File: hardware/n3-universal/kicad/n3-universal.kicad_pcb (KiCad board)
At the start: 2 copper layers, 278 x 120 mm, 131 parts, among them J1 Bornier_5.08, J10 JST-XH, J11 Bornier_5.08, J12 Bornier_5.08, J13 Support OLED, J14 Support I2C ext, J15 Header servo, J16 Header servo, J17 Header service, J18 Bornier_5.08, J19 Bornier_5.08, J2 Jack 5.5/2.1, J20 Header alim, J21 Support I2C libre, J22 Support I2C libre, J23 Bornier_5.08, J24 Bornier_5.08, J25 Bornier_5.08, J26 Bornier_5.08, J27 Bornier_5.08, J28 Support I2C libre, J29 JST-XH, J3 Bornier_5.08, J30 JST-XH, J31 Bornier_5.08, J32 Bornier_5.08, J33 Bornier_5.08, J34 Bornier_5.08, J35 Support module microSD, J36 Bornier_5.08, J37 Bornier_5.08, J4 Bornier_5.08, J5 Bornier_5.08, J6 Bornier_5.08, J7 JST-XH, J8 JST-XH, J9 JST-XH, K1 SRD-05VDC-SL-C, K2 SRD-05VDC-SL-C, K3 SRD-05VDC-SL-C, K4 SRD-05VDC-SL-C, K5 SRD-05VDC-SL-C, K6 SRD-05VDC-SL-C, Q1 BC337-40, Q10 BC337-40, Q11 NDP6020P, Q2 BC337-40, Q3 BC337-40, Q4 BC337-40, Q5 BC337-40, Q6 BC337-40, Q7 NDP6020P, Q8 BC337-40, Q9 BS250

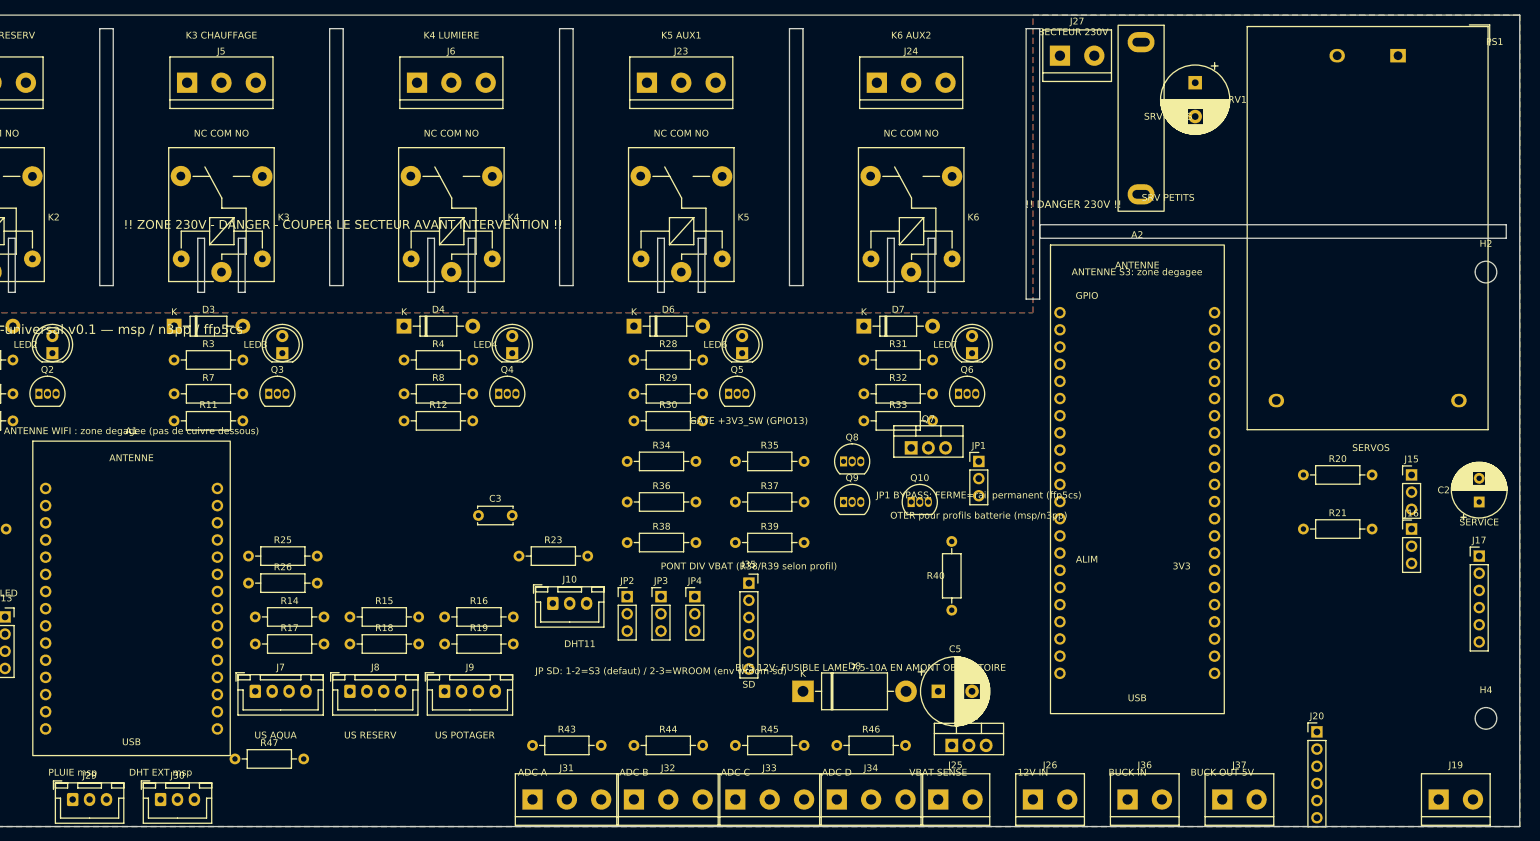
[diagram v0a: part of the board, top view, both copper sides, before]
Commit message: fix(n3-universal): géométrie secteur sans croisement, contour réparé, passe de placement complète
PSU : J27/F1/RV1 hors du corps du Hi-Link (décalé à x303), pistes L/N/LF
redessinées sans croisement ni court (varistance re-câblée N/LF), fente
frontière y71-73 disjointe de la fente verticale (contour valide). ~30
repositionnements sur courtyards réels (rangée basse de borniers y151,
colonne gate/diviseur/SD décalée hors des canaux relais 5/6 et du bloc DHT,
servos/J17/J20 rive droite, trous de fixation déplacés hors zone secteur).
ERC 0 erreur, garde anti-dérive vert, 1 seul avertissement de recouvrement
résiduel corrigé. Routage v2 en cours.

Co-Authored-By: Claude <noreply@anthropic.com>
Claude-Session: https://claude.ai/code/session_01HcxShQb65yktRwp31wBq9q
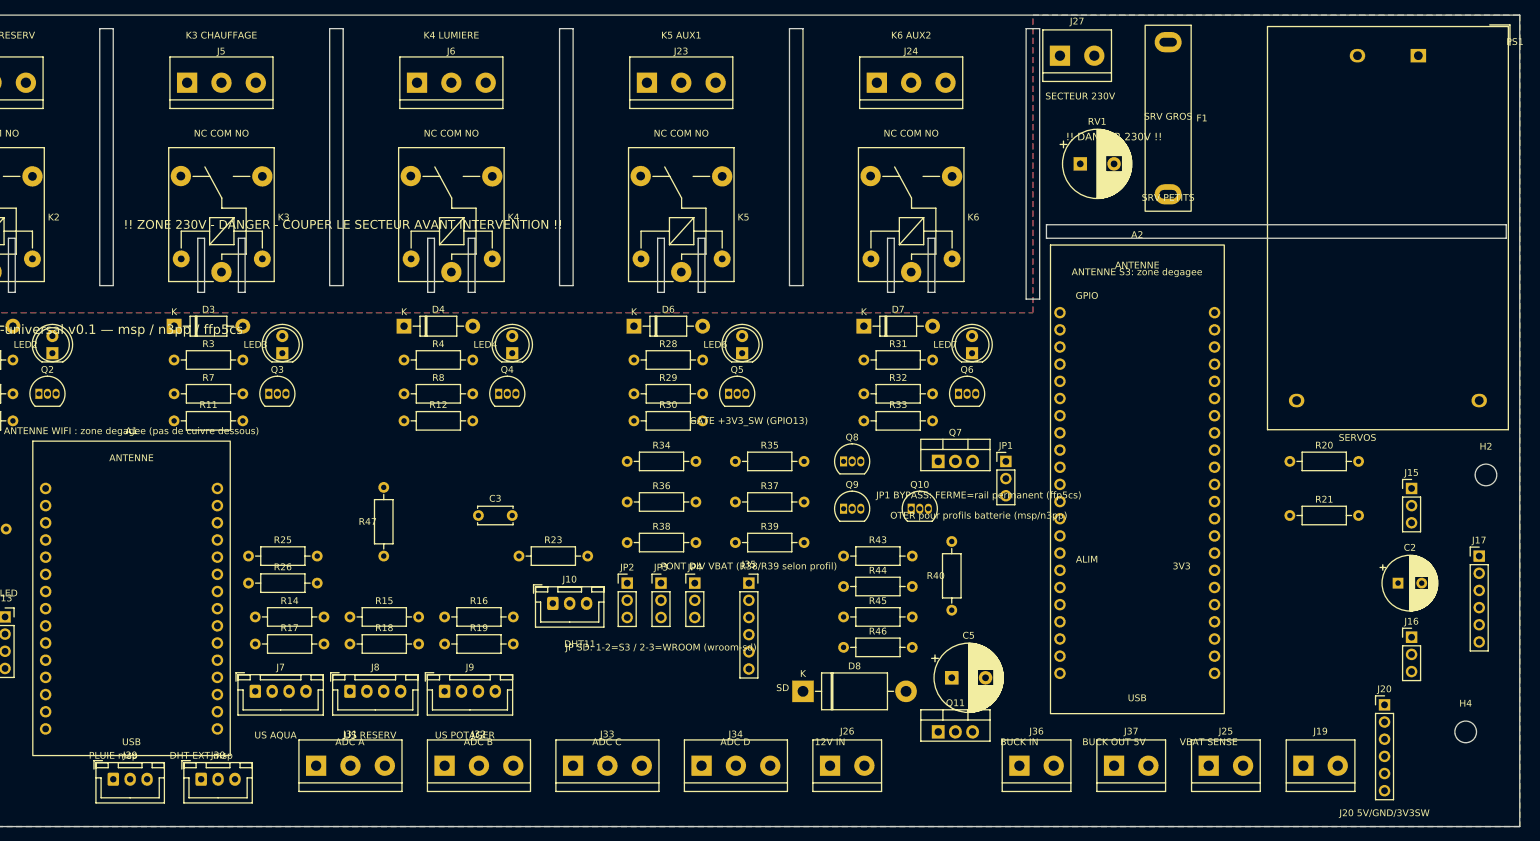
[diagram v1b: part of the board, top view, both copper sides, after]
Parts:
- moved R43 53.9 mm to (218.0, 120.0)
- moved J25 40.3 mm to (272.0, 151.0)
- moved R44 38.9 mm to (218.0, 124.5)
- moved R47 37.2 mm to (150.0, 120.0), turned to 90 degrees
- moved J31 32.4 mm to (140.0, 151.0)
- moved J26 30.4 mm to (216.0, 151.0)
- moved H2 30.0 mm to (313.0, 108.0)
- moved J32 28.4 mm to (159.0, 151.0)
- moved R45 24.8 mm to (218.0, 129.0)
- moved J33 24.5 mm to (178.0, 151.0)
- moved RV1 20.8 mm to (253.0, 62.0), turned to 0 degrees
- moved J19 20.6 mm to (286.0, 151.0)
- moved J34 20.6 mm to (197.0, 151.0)
- moved C2 17.0 mm to (300.0, 124.0), turned to 0 degrees
- moved J36 16.8 mm to (244.0, 151.0)
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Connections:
- RV1 pad 1: MAINS_LF -> MAINS_N
- RV1 pad 2: MAINS_N -> MAINS_LF
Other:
- outline, holes or cut-outs redrawn
- board text added: "J20 5V/GND/3V3SW"
- board text added: "JP SD: 1-2=S3 / 2-3=WROOM (wroom-sd)"
- board text removed: "JP SD: 1-2=S3 (defaut) / 2-3=WROOM (env wroom-sd)"
- board text removed: "SERVICE"

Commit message: fix(n3-universal): amorces SEED_TRACKS (port I2C J14/C4 pincé) + C5 hors du courtyard Q11
Co-Authored-By: Claude <noreply@anthropic.com>
Claude-Session: https://claude.ai/code/session_01HcxShQb65yktRwp31wBq9q
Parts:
- moved C5 2.00 mm to (234.0, 136.0)
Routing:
- net +3V3_SW: track 0.00 -> 7.00 mm
- net I2C_SDA: track 0.00 -> 3.50 mm
- net I2C_SCL: track 0.00 -> 3.50 mm

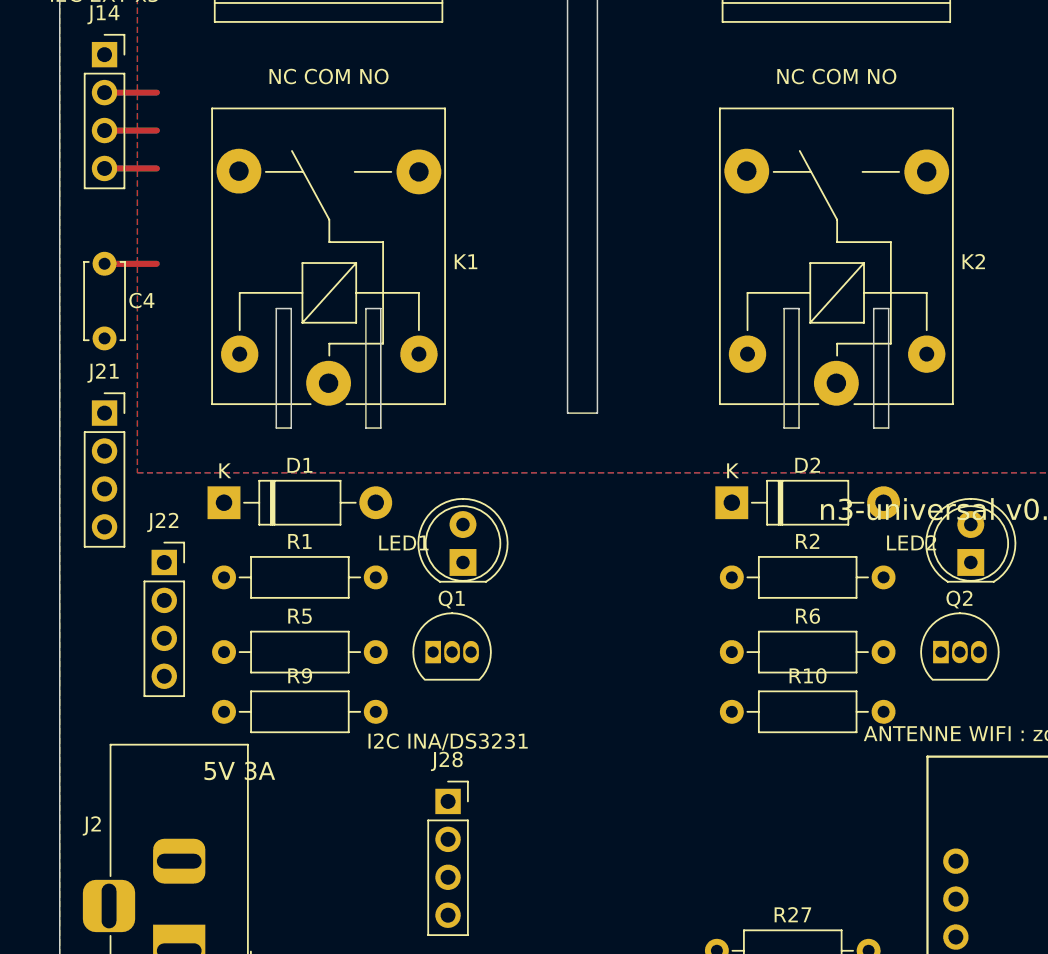
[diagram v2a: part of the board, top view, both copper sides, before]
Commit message: fix(n3-universal): colonne I2C gauche câblée en dur + échappée EN (SEED_TRACKS v2)
Co-Authored-By: Claude <noreply@anthropic.com>
Claude-Session: https://claude.ai/code/session_01HcxShQb65yktRwp31wBq9q
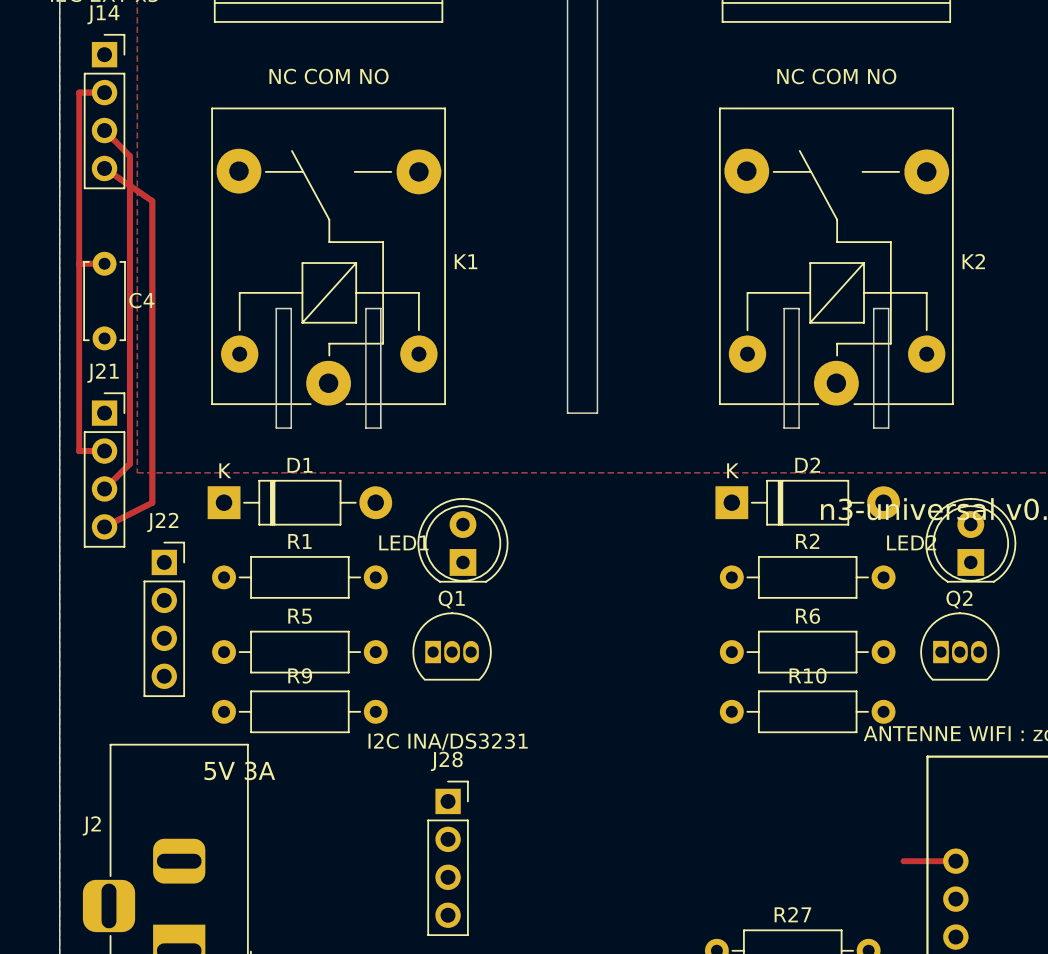
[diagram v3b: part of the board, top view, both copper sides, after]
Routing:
- net I2C_SDA: track 3.50 -> 27.7 mm
- net +3V3_SW: track 7.00 -> 29.1 mm
- net I2C_SCL: track 3.50 -> 25.4 mm
- net EN: track 0.00 -> 3.50 mm
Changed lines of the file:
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@@
 			(layer "F.Fab")
 		)
-		(fp_text user "1"
-			(at 0 -2.3 0)
+		(fp_text user "${REFERENCE}"
+			(at 7.1 0.025 0)
 			(layer "F.Fab")
 			(effects
@@
 			)
 		)
-		(fp_text user "${REFERENCE}"
-			(at 7.1 0.025 0)
+		(fp_text user "1"
+			(at 0 -2.3 0)
 			(layer "F.Fab")
 			(effects
@@
 			)
 		)
-		(fp_text user "${REFERENCE}"
-			(at 5.47 0 0)
+		(fp_text user "K"
+			(at 0 -2.1 0)
 			(layer "F.Fab")
 			(effects
@@
 			)
 		)
-		(fp_text user "K"
-			(at 0 -2.1 0)
+		(fp_text user "${REFERENCE}"
+			(at 5.47 0 0)
 			(layer "F.Fab")
 			(effects
@@
 			)
 		)
-		(fp_text user "K"
-			(at 0 -2.1 0)
+		(fp_text user "${REFERENCE}"
+			(at 5.47 0 0)
 			(layer "F.Fab")
 			(effects
@@
 			)
 		)
-		(fp_text user "${REFERENCE}"
-			(at 5.47 0 0)
+		(fp_text user "K"
+			(at 0 -2.1 0)
 			(layer "F.Fab")
 			(effects
@@
 			)
 		)
-		(fp_text user "${REFERENCE}"
-			(at 8.3325 0 0)
+		(fp_text user "K"
+			(at 0 -2.6 0)
 			(layer "F.Fab")
 			(effects
@@
 			)
 		)
-		(fp_text user "K"
-			(at 0 -2.6 0)
+		(fp_text user "${REFERENCE}"
+			(at 8.3325 0 0)
 			(layer "F.Fab")
 			(effects
@@
 			(layer "F.Fab")
 		)
-		(fp_text user "${REFERENCE}"
-			(at 7.1 0.025 0)
+		(fp_text user "1"
+			(at 0 -2.3 0)
 			(layer "F.Fab")
 			(effects
@@
 			)
 		)
-		(fp_text user "1"
-			(at 0 -2.3 0)
+		(fp_text user "${REFERENCE}"
+			(at 7.1 0.025 0)
 			(layer "F.Fab")
 			(effects
@@
 			)
 		)
-		(fp_text user "K"
-			(at 0 -2.1 0)
+		(fp_text user "${REFERENCE}"
+			(at 5.47 0 0)
 			(layer "F.Fab")
 			(effects
@@
 			)
 		)
-		(fp_text user "${REFERENCE}"
-			(at 5.47 0 0)
+		(fp_text user "K"
+			(at 0 -2.1 0)
 			(layer "F.Fab")
 			(effects
@@
 			(layer "F.Fab")
 		)
-		(fp_text user "1"
-			(at 0 -2.3 0)
+		(fp_text user "${REFERENCE}"
+			(at 7.1 0.025 0)
 			(layer "F.Fab")
 			(effects
@@
 			)
 		)
-		(fp_text user "${REFERENCE}"
-			(at 7.1 0.025 0)
+		(fp_text user "1"
+			(at 0 -2.3 0)
 			(layer "F.Fab")
 			(effects
@@
 			(layer "F.CrtYd")
 		)
-		(fp_text user "USB"
-			(at 12.7 37.5 0)
+		(fp_text user "ANTENNE"
+			(at 12.7 -4.5 0)
 			(layer "F.SilkS")
 			(effects
@@
 			)
 		)
-		(fp_text user "ANTENNE"
-			(at 12.7 -4.5 0)
+		(fp_text user "USB"
+			(at 12.7 37.5 0)
 			(layer "F.SilkS")
 			(effects
@@
 			)
 		)
-		(fp_text user "${REFERENCE}"
-			(at 5.47 0 0)
+		(fp_text user "K"
+			(at 0 -2.1 0)
 			(layer "F.Fab")
 			(effects
@@
 			)
 		)
-		(fp_text user "K"
-			(at 0 -2.1 0)
+		(fp_text user "${REFERENCE}"
+			(at 5.47 0 0)
 			(layer "F.Fab")
 			(effects
@@
 			)
 		)
-		(fp_text user "${REFERENCE}"
-			(at 8.3325 0 0)
+		(fp_text user "K"
+			(at 0 -2.6 0)
 			(layer "F.Fab")
 			(effects
@@
 			)
 		)
-		(fp_text user "K"
-			(at 0 -2.6 0)
+		(fp_text user "${REFERENCE}"
+			(at 8.3325 0 0)
 			(layer "F.Fab")
 			(effects
@@
 			(layer "F.Fab")
 		)
-		(fp_text user "1"
-			(at 0 -2.3 0)
+		(fp_text user "${REFERENCE}"
+			(at 7.1 0.025 0)
 			(layer "F.Fab")
 			(effects
@@
 			)
 		)
-		(fp_text user "${REFERENCE}"
-			(at 7.1 0.025 0)
+		(fp_text user "1"
+			(at 0 -2.3 0)
 			(layer "F.Fab")
 			(effects
@@
 	)
 	(segment
+		(start 41.3 82.54)
+		(end 43 82.54)
+		(width 0.4)
+		(layer "F.Cu")
+		(net 2)
+	)
+	(segment
+		(start 41.3 70)
+		(end 41.3 82.54)
+		(width 0.4)
+		(layer "F.Cu")
+		(net 2)
+	)
+	(segment
 		(start 43 58.54)
-		(end 46.5 58.54)
+		(end 41.3 58.54)
+		(width 0.4)
+		(layer "F.Cu")
+		(net 2)
+	)
+	(segment
+		(start 41.3 70)
+		(end 43 70)
 		(width 0.4)
 		(layer "F.Cu")
@@
 	)
 	(segment
-		(start 43 70)
-		(end 46.5 70)
+		(start 41.3 58.54)
+		(end 41.3 70)
 		(width 0.4)
 		(layer "F.Cu")
@@
 	)
 	(segment
+		(start 96.5 110)
+		(end 100 110)
+		(width 0.4)
+		(layer "F.Cu")
+		(net 11)
+	)
+	(segment
+		(start 44.7 83.4)
+		(end 43 85.08)
+		(width 0.4)
+		(layer "F.Cu")
+		(net 16)
+	)
+	(segment
+		(start 44.7 62.8)
+		(end 44.7 83.4)
+		(width 0.4)
+		(layer "F.Cu")
+		(net 16)
+	)
+	(segment
 		(start 43 61.08)
-		(end 46.5 61.08)
+		(end 44.7 62.8)
 		(width 0.4)
 		(layer "F.Cu")
@@
 	)
 	(segment
+		(start 46.2 86)
+		(end 43 87.62)
+		(width 0.4)
+		(layer "F.Cu")
+		(net 17)
+	)
+	(segment
 		(start 43 63.62)
-		(end 46.5 63.62)
+		(end 46.2 65.8)
+		(width 0.4)
+		(layer "F.Cu")
+		(net 17)
+	)
+	(segment
+		(start 46.2 65.8)
+		(end 46.2 86)
 		(width 0.4)
 		(layer "F.Cu")
